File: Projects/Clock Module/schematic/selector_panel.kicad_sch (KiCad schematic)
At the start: 18 parts, among them SW4 SW_Push, SW5 SW_Push, SW6 SW_Push, U11 74LS73, U12 74LS73, U13 74LS04, U14 74LS32, U4 74LS04, U6 74LS32

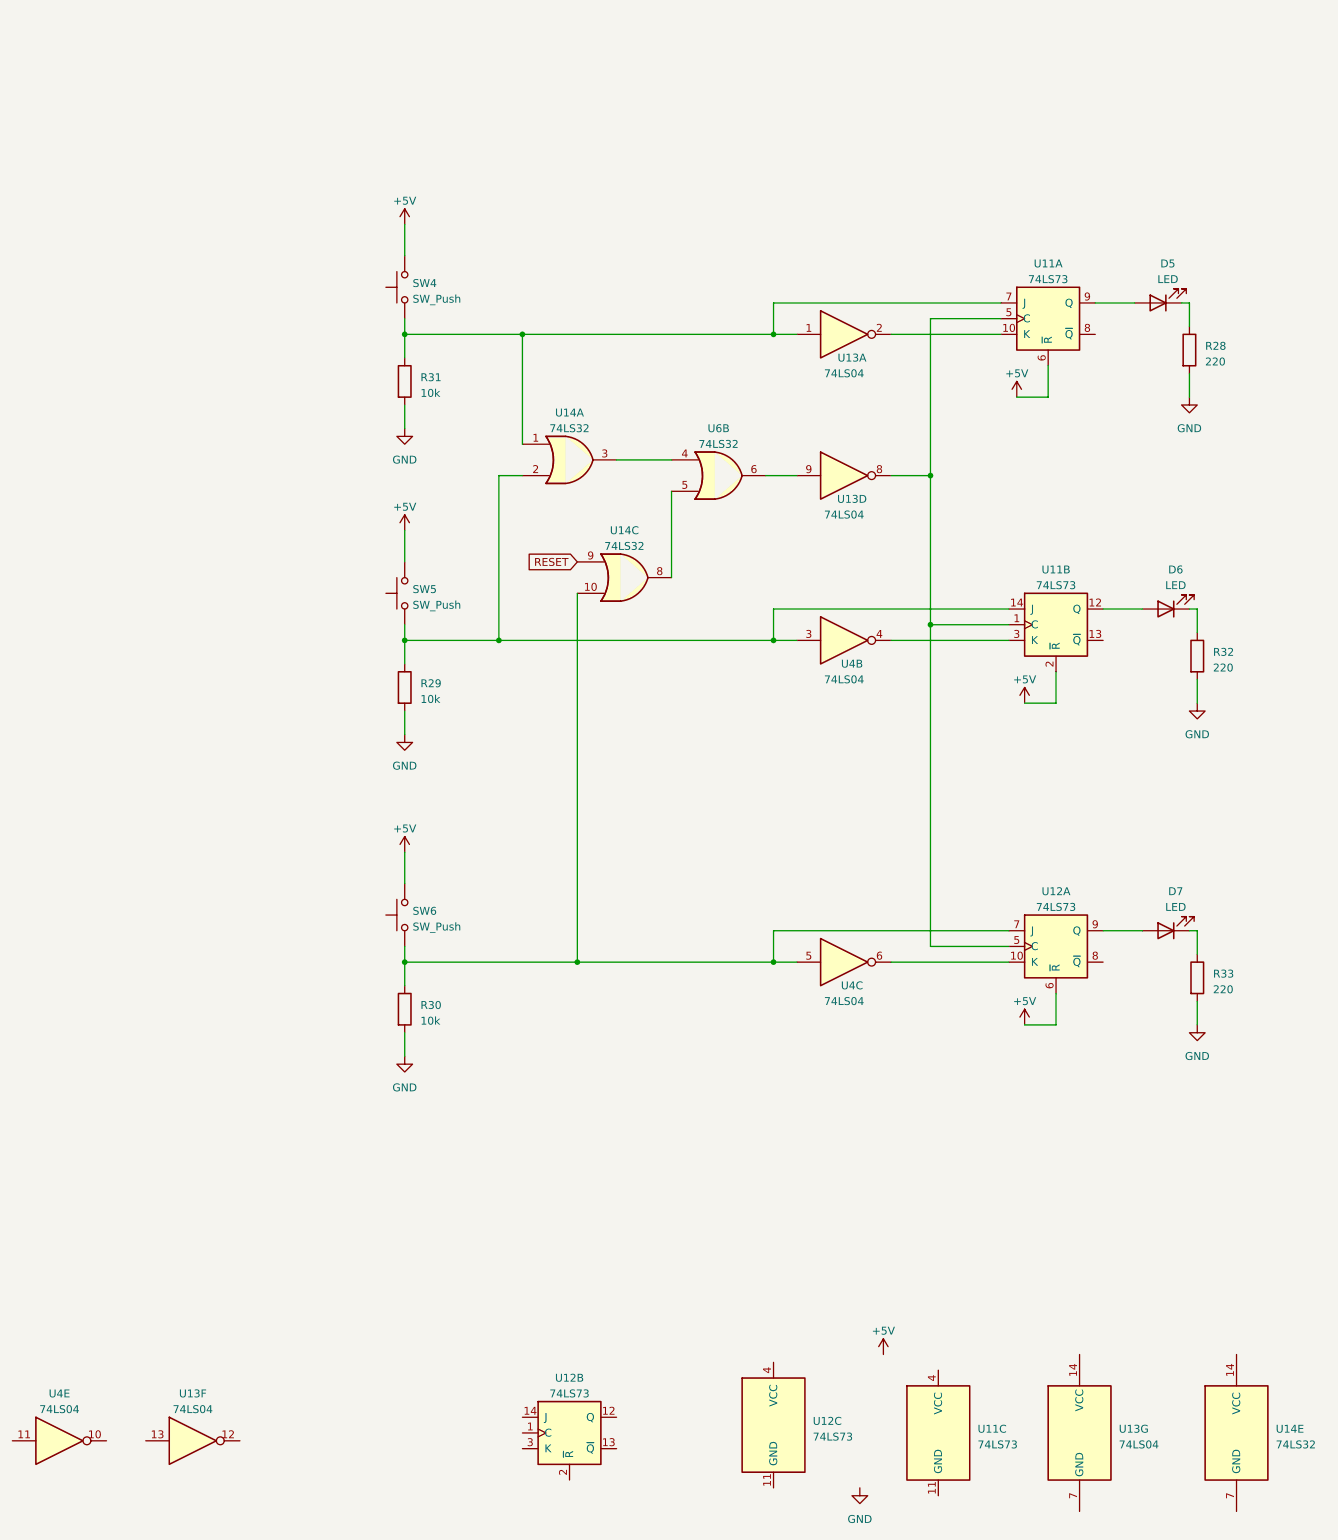
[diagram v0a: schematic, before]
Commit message: Updated clock to use the selector panel
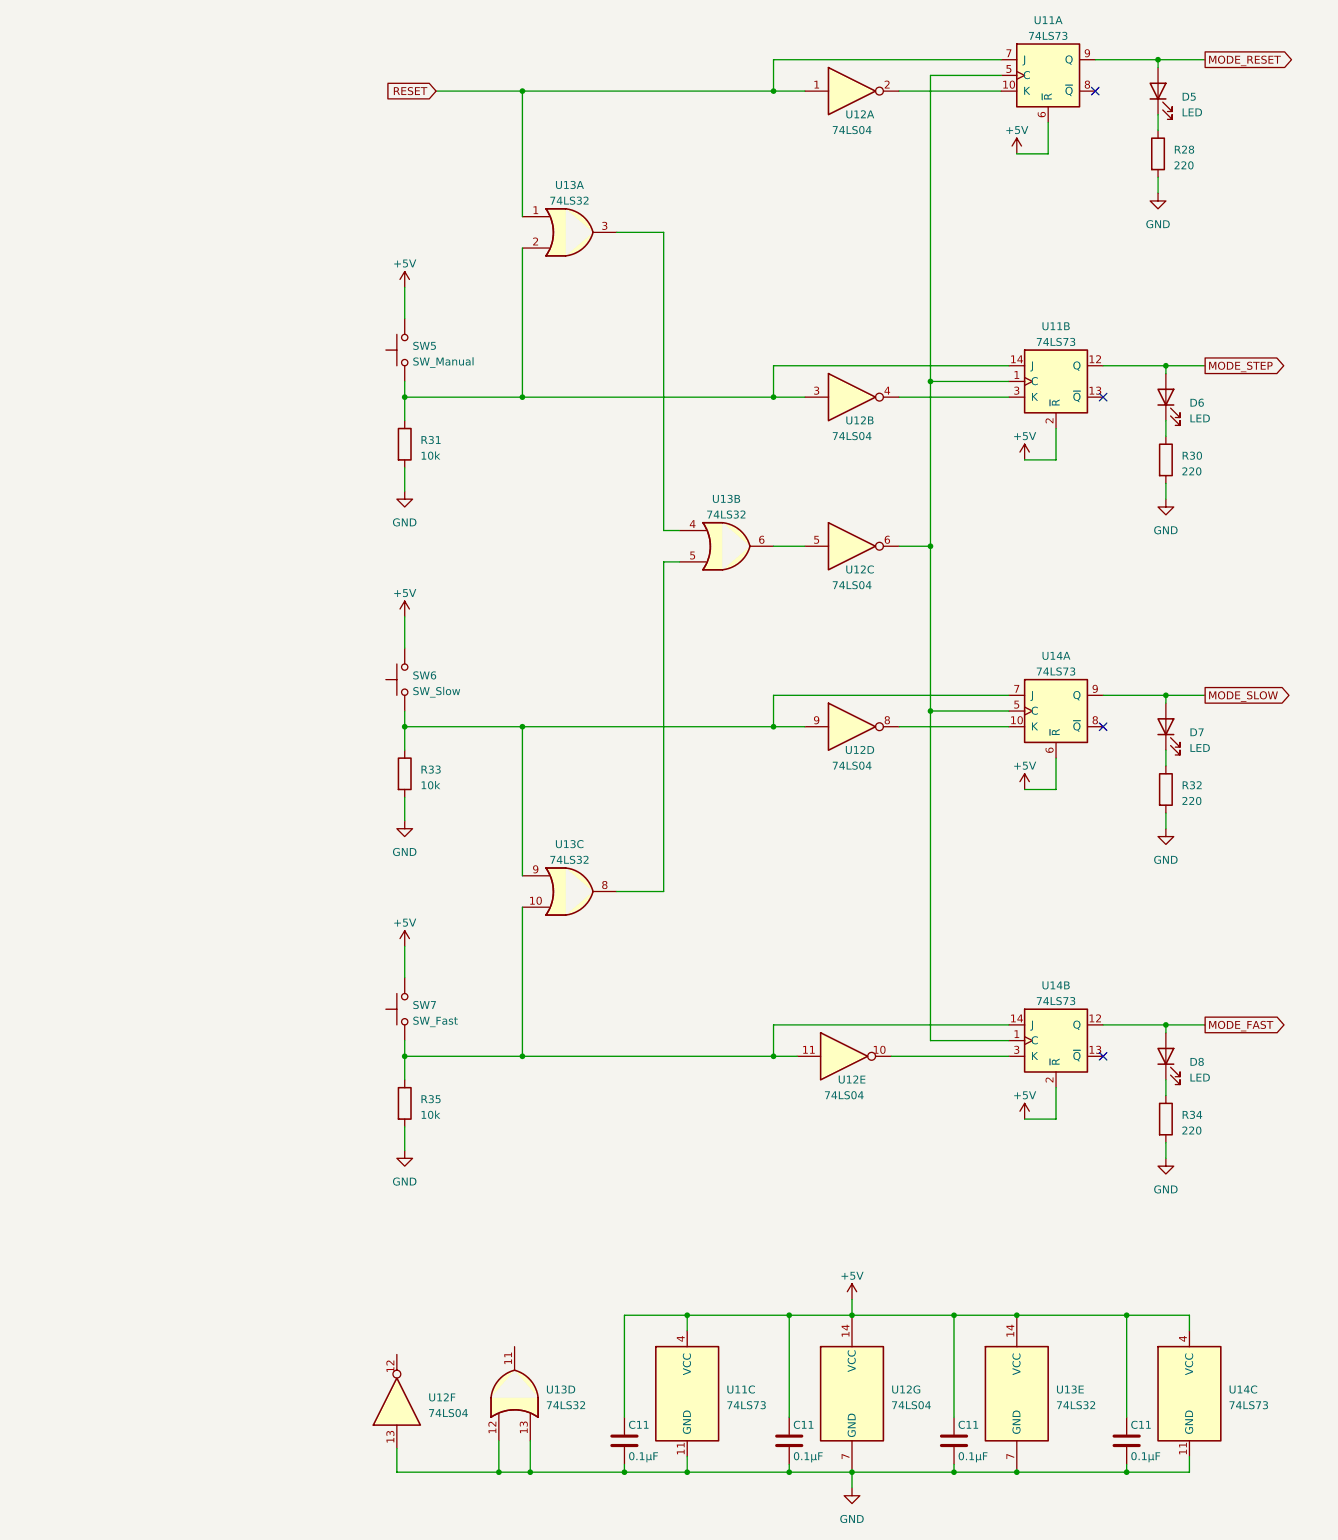
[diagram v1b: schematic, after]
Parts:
- removed R31: 10k, symbol Device:R
- removed SW4: SW_Push, symbol Switch:SW_Push
- removed unit 2 of U12
- removed unit 6 of U13
- added C11 (x4): 0.1µF, Capacitor_THT:C_Disc_D4.3mm_W1.9mm_P5.00mm, symbol Device:C
- added D7: LED, symbol Device:LED
- added R30, R34: 220, symbol Device:R
- added SW6: SW_Slow, symbol Switch:SW_Push
- added unit 4 of U12
- added unit 4 of U13
- added unit 1 of U14
- R33: value 220 -> 10k
- SW5: value SW_Push -> SW_Manual
- SW7: renamed from SW6; value SW_Push -> SW_Fast
- renumbered D7 to D8, R29 to R31, R30 to R35, U13 to U12, U4 to U12, U14 to U13, U6 to U13, U12 to U14
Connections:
- net +5V: now also U11.4 (VCC), U12.14 (VCC), U13.14 (VCC), U14.2 (~{R}), U14.4 (VCC), C11.1, C11.1, C11.1, C11.1, SW6.2, U14.6 (~{R}); no longer U14.6 (~{R})
- net GND: now also U11.11 (GND), U12.13, U12.7 (GND), U13.7 (GND), U14.11 (GND), C11.2, C11.2, C11.2, C11.2, R30.2, R34.2, U13.12, U13.13
- net RESET: now also U11.7 (J), U12.1, U13.1; no longer U13.9
- net at U11.1 (C), U11.5 (C): now also U12.6, U14.1 (C), U14.5 (C); no longer U12.8, U14.5 (C)
- net at U13.6: now also U12.5; no longer U12.9
- net MODE_STEP: now reaches D6.2 (A), U11.12 (Q)
- net at R33.1: now also U13.9, SW6.1, U12.9, U14.7 (J); no longer D8.1 (K)
- net at R32.1: now also D7.1 (K); no longer D6.1 (K)
- net at R35.1, SW7.1, U13.10: now also U12.11, U14.14 (J); no longer U12.5, U14.7 (J)
- net MODE_RESET: now reaches D5.2 (A), U11.9 (Q)
- net MODE_FAST: now reaches D8.2 (A)
- net MODE_FAST: now also U14.12 (Q); no longer U14.9 (Q)
- new net: U12.8, U14.10 (K)
- new net: D6.1 (K), R30.1
- new net: U12.10, U14.3 (K)
- new net: D8.1 (K), R34.1
- new net MODE_SLOW: D7.2 (A), U14.9 (Q)
- no-connect marks 0 -> 4
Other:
- moved on the sheet: D5, D6, D8, R28, R31, R35, SW5, SW7, U11A, U11B, U11C, U12A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
